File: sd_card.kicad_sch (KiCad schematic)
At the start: 0 parts

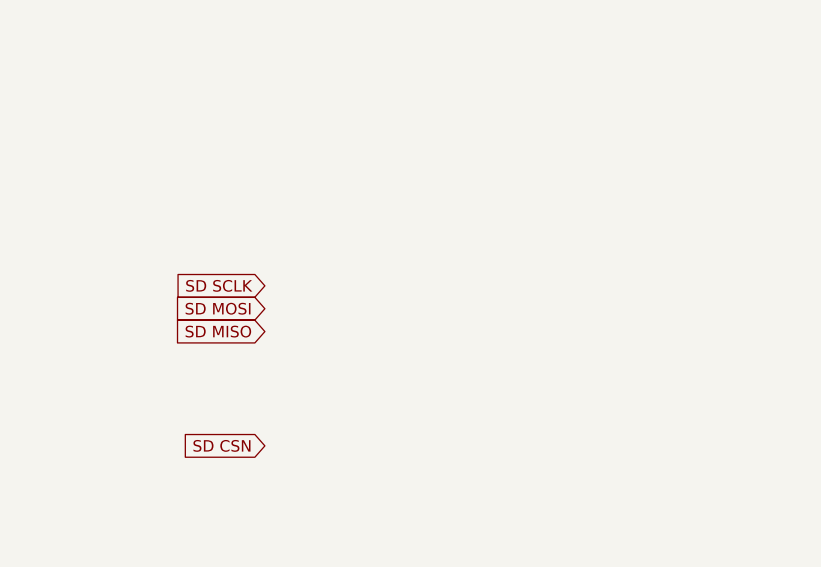
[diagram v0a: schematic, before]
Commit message: Added pull ups to SD data lines in line with SD standard
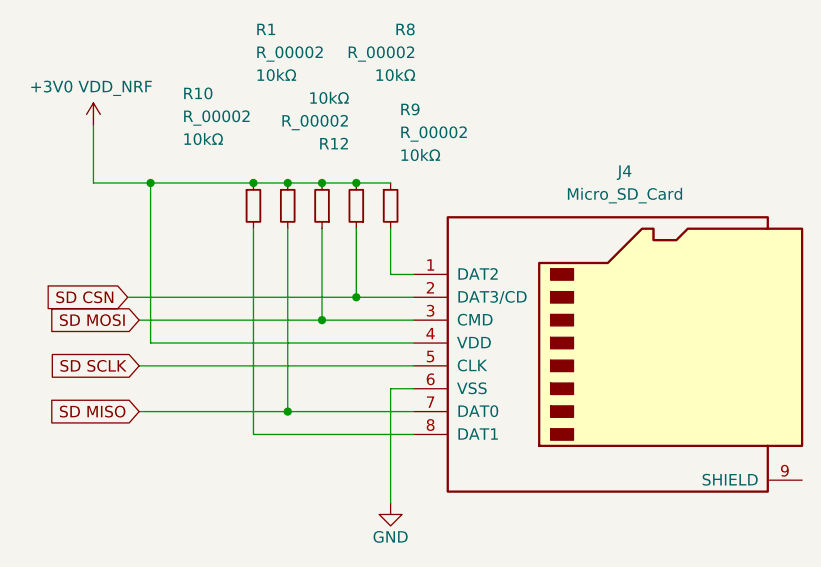
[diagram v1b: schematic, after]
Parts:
- added J4: Micro_SD_Card, symbol mic_patch_parts:Micro_SD_Card
- added R1, R10, R12, R8, R9: R_00002, symbol mic_patch_parts:R_00003
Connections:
- net SD CSN: now also J4.2 (DAT3/CD), R8.1
- net SD MISO: now also J4.7 (DAT0), R1.2
- net SD MOSI: now also J4.3 (CMD), R12.1
- net SD SCLK: now also J4.5 (CLK)
- new net: J4.1 (DAT2), R9.2
- new net: J4.8 (DAT1), R10.2
- new net +3V0 VDD_NRF: J4.4 (VDD), R1.1, R10.1, R12.2, R8.2, R9.1
- new net GND: J4.6 (VSS)

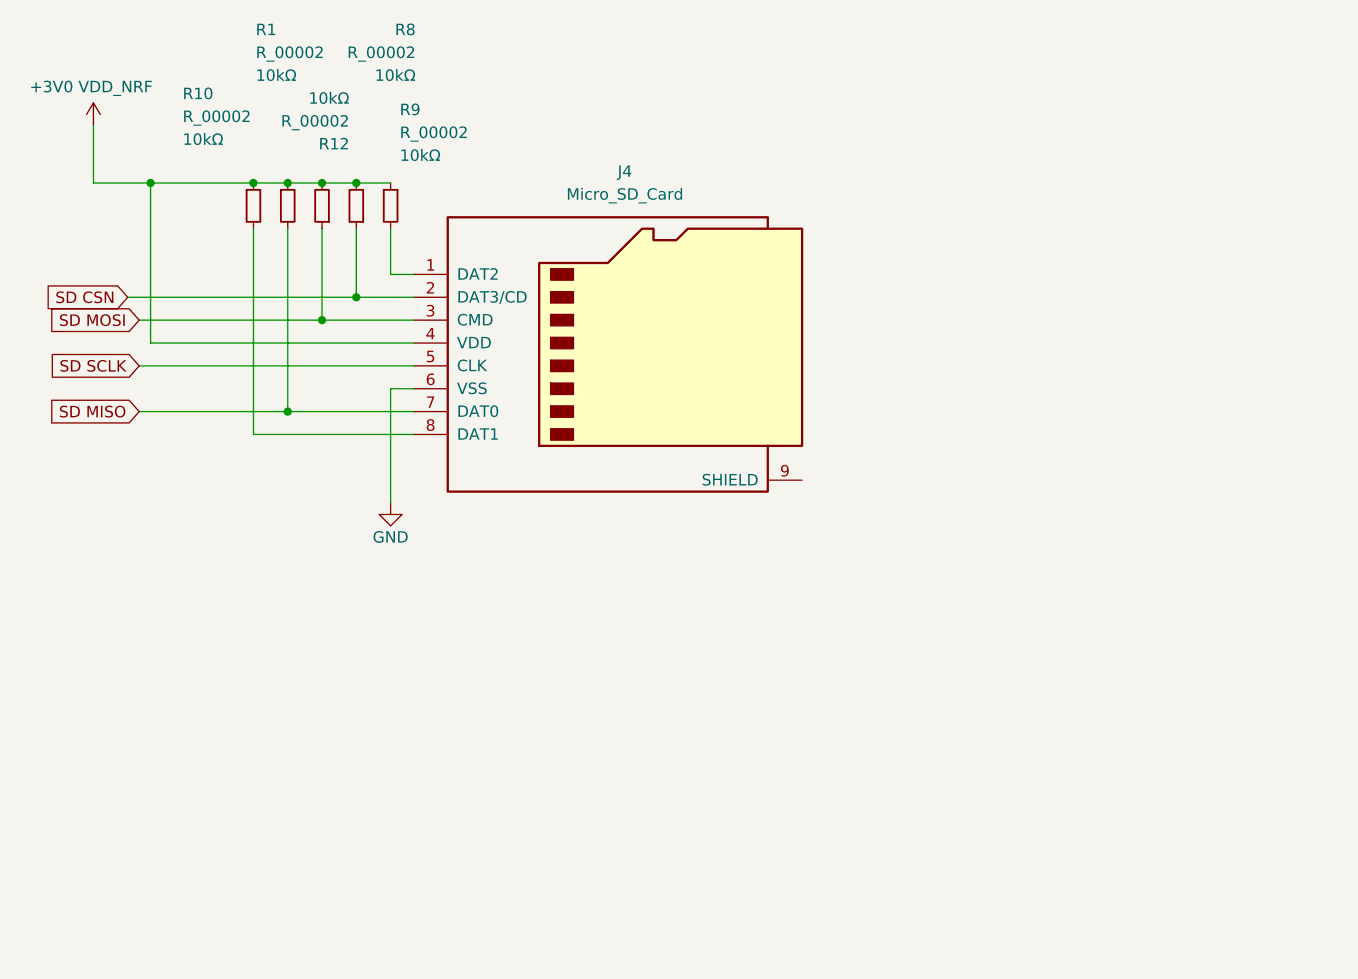
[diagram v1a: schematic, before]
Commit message: Added SD card ESD protection
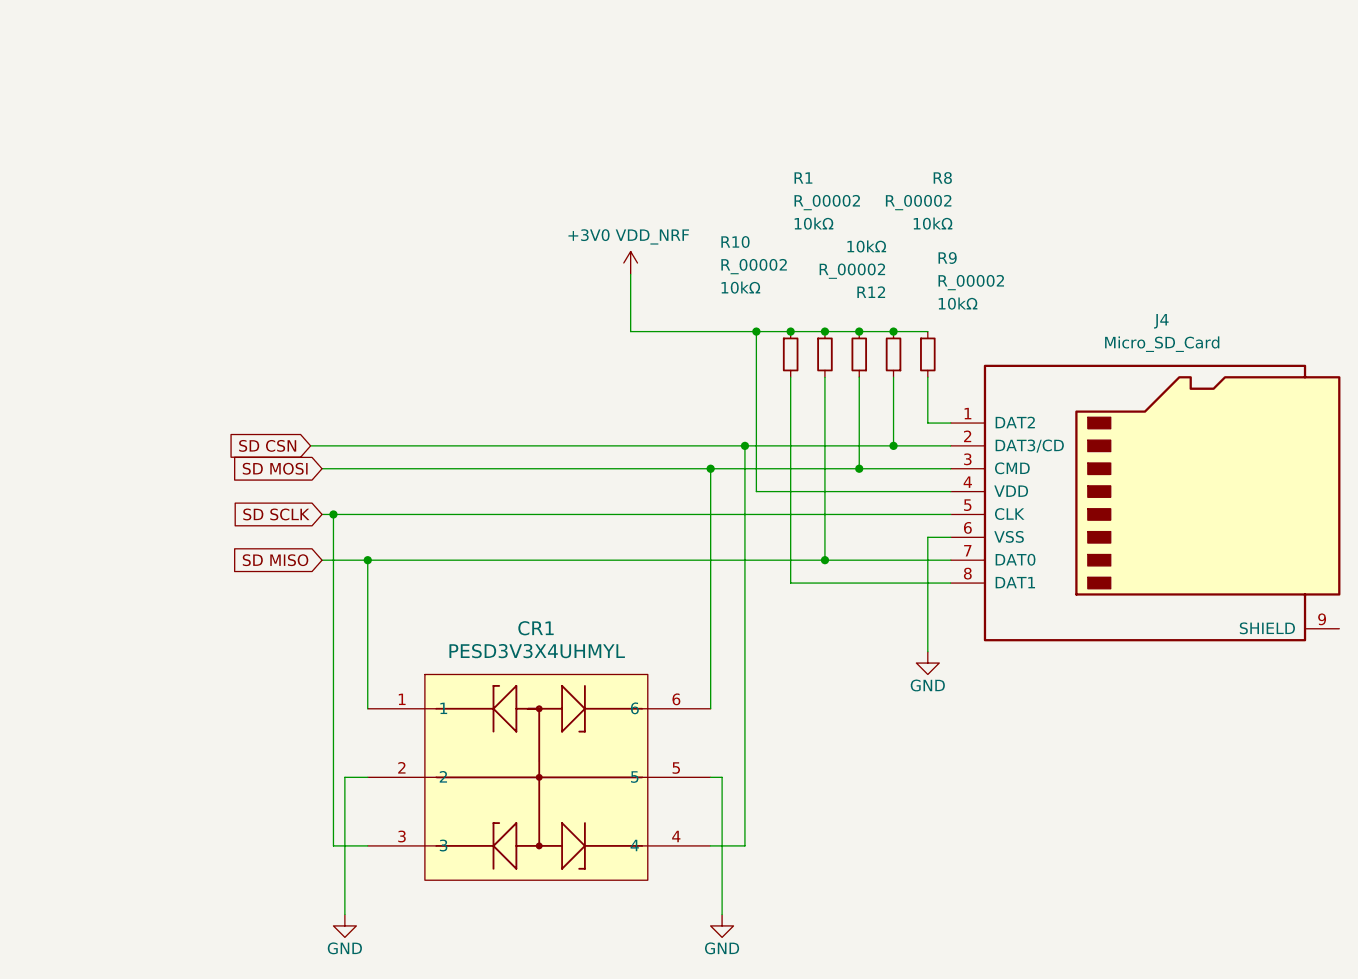
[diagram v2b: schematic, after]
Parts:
- added CR1: PESD3V3X4UHMYL, DFN1308-6_SOT8006_NEX, symbol mic_patch_parts:PESD3V3X4UHMYL
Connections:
- net GND: now also CR1.2, CR1.5
- net SD CSN: now also CR1.4
- net SD MISO: now also CR1.1
- net SD MOSI: now also CR1.6
- net SD SCLK: now also CR1.3
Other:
- moved on the sheet: J4, R1, R10, R12, R8, R9

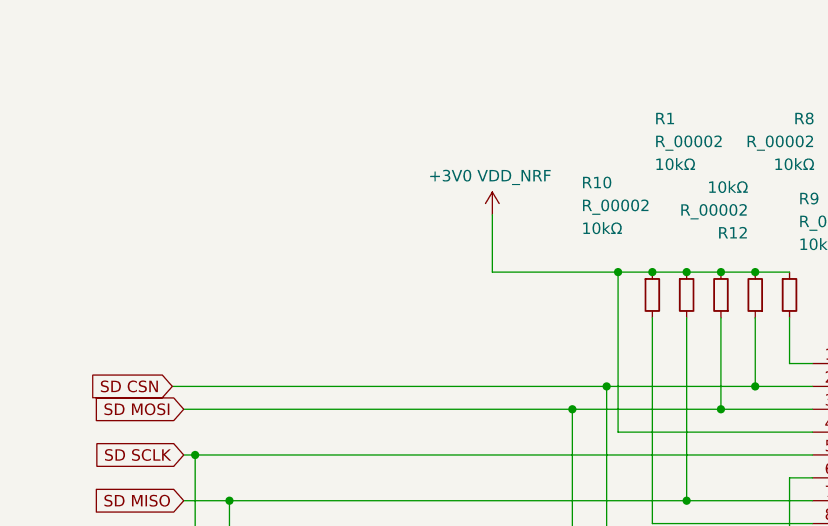
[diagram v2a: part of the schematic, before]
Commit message: added decoupling to  micro SD card
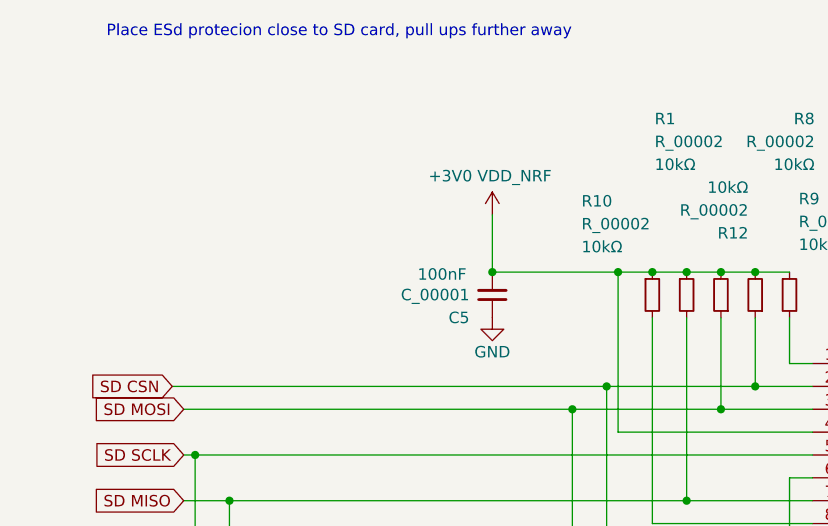
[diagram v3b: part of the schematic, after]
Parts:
- added C5: C_00001, symbol mic_patch_parts:C_00001
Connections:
- net +3V0 VDD_NRF: now also C5.2
- net GND: now also C5.1
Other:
- note added: "Place ESd protecion close to SD card, pull ups further away"
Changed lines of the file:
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@@
+	)
+	(junction
+		(at 87.63 60.96)
+		(diameter 0)
+		(color 0 0 0 0)
 	)
 	(junction
@@
 			(width 0)
 			(type default)
+		)
+	)
+	(text "Place ESd protecion close to SD card, pull ups further away"
+		(exclude_from_sim no)
+		(at 70.612 34.29 0)
+		(effects
+			(font
+				(size 1.27 1.27)
+			)
 		)
 	)
@@
 				(path "/5448a297-4261-40a5-8009-47199bfe22cb/800536da-ce80-4a29-90e4-a5031f507197"
 					(reference "#PWR012")
+					(unit 1)
+				)
+			)
+		)
+	)
+	(symbol
+		(lib_id "mic_patch_parts:C_00001")
+		(at 87.63 63.5 180)
+		(unit 1)
+		(exclude_from_sim no)
+		(in_bom yes)
+		(on_board yes)
+		(dnp no)
+		(fields_autoplaced yes)
+		(property "Reference" "C5"
+			(at 85.09 66.04 0)
+			(do_not_autoplace yes)
+			(effects
+				(font
+					(size 1.27 1.27)
+				)
+				(justify left)
+			)
+		)
+		(property "Value" "C_00001"
+			(at 85.09 63.5 0)
+			(do_not_autoplace yes)
+			(effects
+				(font
+					(size 1.27 1.27)
+				)
+				(justify left)
+			)
+		)
+		(property "Footprint" ""
+			(at 113.03 62.23 0)
+			(effects
+				(font
+					(size 1.27 1.27)
+				)
+				(hide yes)
+			)
+		)
+		(property "Datasheet" "~"
+			(at 87.63 63.5 0)
+			(effects
+				(font
+					(size 1.27 1.27)
+				)
+				(hide yes)
+			)
+		)
+		(property "Description" "100nF"
+			(at 82.042 61.214 0)
+			(do_not_autoplace yes)
+			(effects
+				(font
+					(size 1.27 1.27)
+				)
+			)
+		)
+		(property "Desc" ""
+			(at 85.09 60.96 0)
+			(do_not_autoplace yes)
+			(effects
+				(font
+					(size 1.27 1.27)
+				)
+				(justify left)
+			)
+		)
+		(property "MPNs" ""
+			(at 109.22 71.12 0)
+			(effects
+				(font
+					(size 1.27 1.27)
+				)
+				(hide yes)
+			)
+		)
+		(property "LCSC PNs" ""
+			(at 107.95 66.04 0)
+			(effects
+				(font
+					(size 1.27 1.27)
+				)
+				(hide yes)
+			)
+		)
+		(pin "1"
+		)
+		(pin "2"
+		)
+		(instances
+			(project "mic_patch_v1"
+				(path "/5448a297-4261-40a5-8009-47199bfe22cb/800536da-ce80-4a29-90e4-a5031f507197"
+					(reference "C5")
 					(unit 1)
 				)
@@
 		(dnp no)
 		(property "Reference" "R10"
-			(at 97.536 51.054 0)
+			(at 97.536 53.086 0)
 			(effects
 				(font
@@
 		)
 		(property "Value" "R_00002"
-			(at 97.536 53.594 0)
+			(at 97.536 55.626 0)
 			(effects
 				(font
@@
 		)
 		(property "Desc" "10kΩ "
-			(at 97.536 56.134 0)
+			(at 97.536 58.166 0)
 			(effects
 				(font
@@
 					(unit 1)
 				)
+			)
+		)
+	)
+	(symbol
+		(lib_id "power:GND")
+		(at 87.63 66.04 0)
+		(unit 1)
+		(exclude_from_sim no)
+		(in_bom yes)
+		(on_board yes)
+		(dnp no)
+		(property "Reference" "#PWR013"
+			(at 87.63 72.39 0)
+			(effects
+				(font
+					(size 1.27 1.27)
+				)
+				(hide yes)
+			)
+		)
+		(property "Value" "GND"
+			(at 87.63 69.85 0)
+			(effects
+				(font
+					(size 1.27 1.27)
+				)
+			)
+		)
+		(property "Footprint" ""
+			(at 87.63 66.04 0)
+			(effects
+				(font
+					(size 1.27 1.27)
+				)
+				(hide yes)
+			)
+		)
+		(property "Datasheet" ""
+			(at 87.63 66.04 0)
+			(effects
+				(font
+					(size 1.27 1.27)
+				)
+				(hide yes)
+			)
+		)
+		(property "Description" "Power symbol creates a global label with name \"GND\" , ground"
+			(at 87.63 66.04 0)
+			(effects
+				(font
+					(size 1.27 1.27)
+				)
+				(hide yes)
+			)
+		)
+		(pin "1"
+		)
+		(instances
+			(project "mic_patch_v1"
+				(path "/5448a297-4261-40a5-8009-47199bfe22cb/800536da-ce80-4a29-90e4-a5031f507197"
+					(reference "#PWR013")
+					(unit 1)
+				)

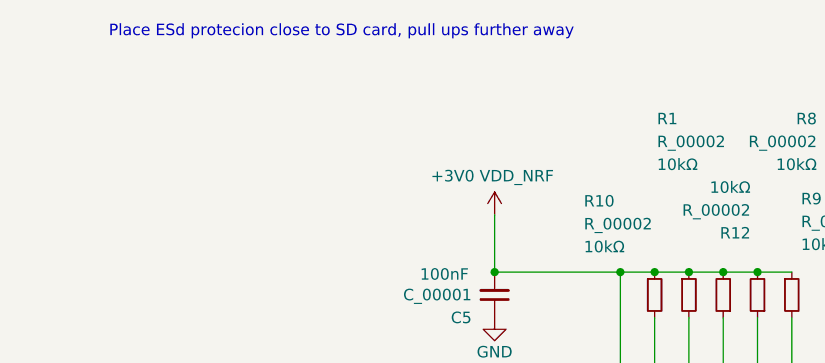
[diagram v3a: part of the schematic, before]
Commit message: changed vterm to 4.25V on the npm1100, added GPIO control of npm1100 BUCK modes
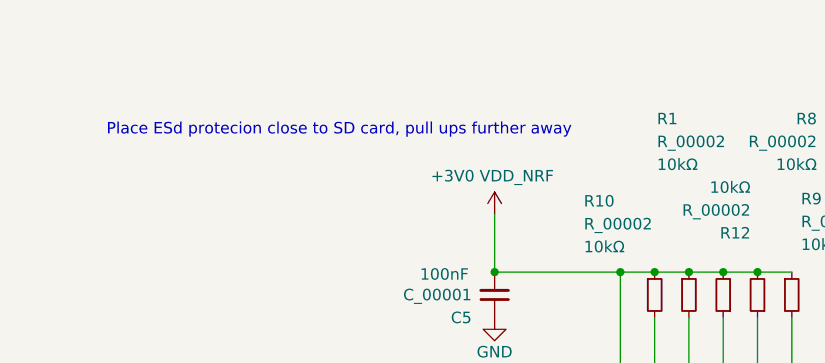
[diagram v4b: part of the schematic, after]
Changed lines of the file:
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@@
 	(text "Place ESd protecion close to SD card, pull ups further away"
 		(exclude_from_sim no)
-		(at 70.612 34.29 0)
+		(at 70.358 45.212 0)
 		(effects
 			(font

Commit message: added schmatic symbols and footprints for key capacitors, selected LCXO crystal to use internal caps
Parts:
- C5: footprint (none) -> Capacitor_SMD:C_0402_1005Metric; LCSC PNs (none) -> C25744; MPNs (none) -> 0402WGF1002TCE
- R1, R10, R12, R8, R9: footprint (none) -> Resistor_SMD:R_0402_1005Metric; LCSC PNs (none) -> C25744; MPNs (none) -> 0402WGF1002TCE
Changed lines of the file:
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@@
 			)
 		)
-		(property "Footprint" ""
+		(property "Footprint" "Capacitor_SMD:C_0402_1005Metric"
 			(at 113.03 62.23 0)
 			(effects
@@
 			)
 		)
-		(property "MPNs" ""
+		(property "MPNs" "0402WGF1002TCE"
 			(at 109.22 71.12 0)
 			(effects
@@
 			)
 		)
-		(property "LCSC PNs" ""
+		(property "LCSC PNs" "C25744"
 			(at 107.95 66.04 0)
 			(effects
@@
 			)
 		)
-		(property "Footprint" ""
+		(property "Footprint" "Resistor_SMD:R_0402_1005Metric"
 			(at 109.22 63.5 0)
 			(effects
@@
 			)
 		)
-		(property "Description" "10kΩ resistor"
+		(property "Description" "10kΩ resistor 0402"
 			(at 109.22 63.5 0)
 			(effects
@@
 			)
 		)
-		(property "MPNs" ""
+		(property "MPNs" "0402WGF1002TCE"
 			(at 109.22 63.5 0)
 			(effects
@@
 			)
 		)
-		(property "LCSC PNs" ""
+		(property "LCSC PNs" "C25744"
 			(at 109.22 63.5 0)
 			(effects
@@
 			)
 		)
-		(property "Footprint" ""
+		(property "Footprint" "Resistor_SMD:R_0402_1005Metric"
 			(at 113.03 63.5 0)
 			(effects
@@
 			)
 		)
-		(property "Description" "10kΩ resistor"
+		(property "Description" "10kΩ resistor 0402"
 			(at 113.03 63.5 0)
 			(effects
@@
 			)
 		)
-		(property "MPNs" ""
+		(property "MPNs" "0402WGF1002TCE"
 			(at 113.03 63.5 0)
 			(effects
@@
 			)
 		)
-		(property "LCSC PNs" ""
+		(property "LCSC PNs" "C25744"
 			(at 113.03 63.5 0)
 			(effects
@@
 			)
 		)
-		(property "Footprint" ""
+		(property "Footprint" "Resistor_SMD:R_0402_1005Metric"
 			(at 105.41 63.5 0)
 			(effects
@@
 			)
 		)
-		(property "Description" "10kΩ resistor"
+		(property "Description" "10kΩ resistor 0402"
 			(at 105.41 63.5 0)
 			(effects
@@
 			)
 		)
-		(property "MPNs" ""
+		(property "MPNs" "0402WGF1002TCE"
 			(at 105.41 63.5 0)
 			(effects
@@
 			)
 		)
-		(property "LCSC PNs" ""
+		(property "LCSC PNs" "C25744"
 			(at 105.41 63.5 0)
 			(effects
@@
 			)
 		)
-		(property "Footprint" ""
+		(property "Footprint" "Resistor_SMD:R_0402_1005Metric"
 			(at 116.84 63.5 0)
 			(effects
@@
 			)
 		)
-		(property "Description" "10kΩ resistor"
+		(property "Description" "10kΩ resistor 0402"
 			(at 116.84 63.5 0)
 			(effects
@@
 			)
 		)
-		(property "MPNs" ""
+		(property "MPNs" "0402WGF1002TCE"
 			(at 116.84 63.5 0)
 			(effects
@@
 			)
 		)
-		(property "LCSC PNs" ""
+		(property "LCSC PNs" "C25744"
 			(at 116.84 63.5 0)
 			(effects
@@
 			)
 		)
-		(property "Footprint" ""
+		(property "Footprint" "Resistor_SMD:R_0402_1005Metric"
 			(at 120.65 63.5 0)
 			(effects
@@
 			)
 		)
-		(property "Description" "10kΩ resistor"
+		(property "Description" "10kΩ resistor 0402"
 			(at 120.65 63.5 0)
 			(effects
@@
 			)
 		)
-		(property "MPNs" ""
+		(property "MPNs" "0402WGF1002TCE"
 			(at 120.65 63.5 0)
 			(effects
@@
 			)
 		)
-		(property "LCSC PNs" ""
+		(property "LCSC PNs" "C25744"
 			(at 120.65 63.5 0)
 			(effects

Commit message: added footprints for every part
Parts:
- CR1: footprint DFN1308-6_SOT8006_NEX -> mic_patch_parts:DFN1308-6_SOT8006_NEX
- J4: footprint (none) -> mic_patch_parts:TF-SMD_TF-017
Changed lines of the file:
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@@
 			)
 		)
-		(property "Footprint" ""
+		(property "Footprint" "mic_patch_parts:TF-SMD_TF-017"
 			(at 175.26 71.12 0)
 			(effects
@@
 			)
 		)
-		(property "Footprint" "DFN1308-6_SOT8006_NEX"
+		(property "Footprint" "mic_patch_parts:DFN1308-6_SOT8006_NEX"
 			(at 88.138 94.488 0)
 			(effects
